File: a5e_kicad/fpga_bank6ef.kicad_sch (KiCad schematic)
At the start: 1 part, among them U7 A5EB013B-B23B

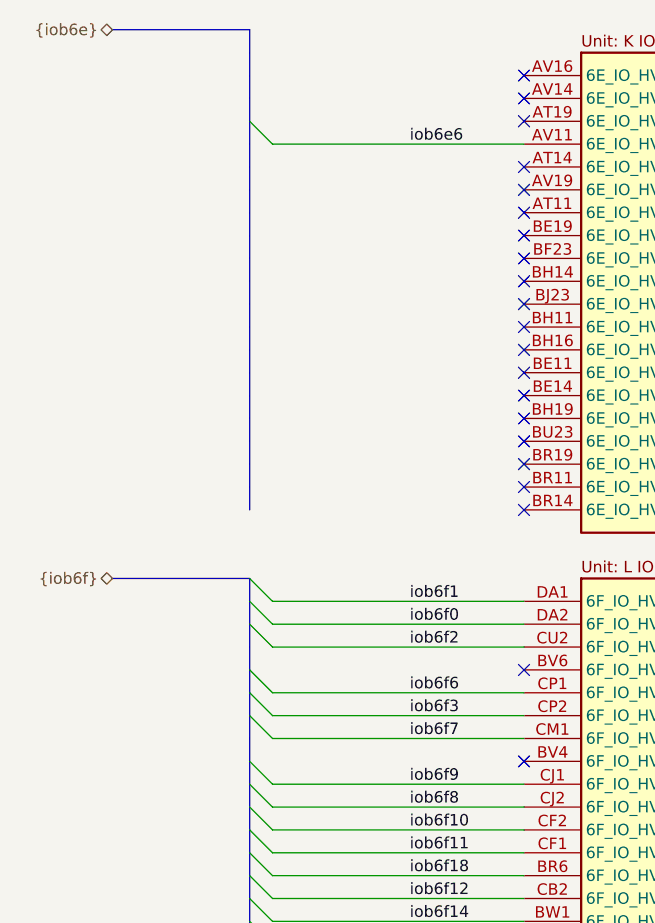
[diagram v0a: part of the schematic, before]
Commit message: Ethernet PHY passives to 0201, R27/R28 to 0402, preliminary RGMII routing
- 31 PHY passives on the hps_ethernet sheet 0402 -> 0201 (C24 22u stays
  0402): 100n C190183, 1u C272877, 27p C85899, 10k C473048,
  330R C516485, 4K7 C270346, 1K5 C270361, 2K49 C473476.
- Refclk bias R27/R28 0201 -> 0402 (C25120, 49.9R); R28 moved 0.1 mm
  to +x to clear the refclk_N meander.
- Preliminary RGMII routing: RX on F.Cu, TX on In2. Group spread
  TX 79 ps (TXD1 longest), RX 44 ps.
- Schematic sheets as saved by eeschema.
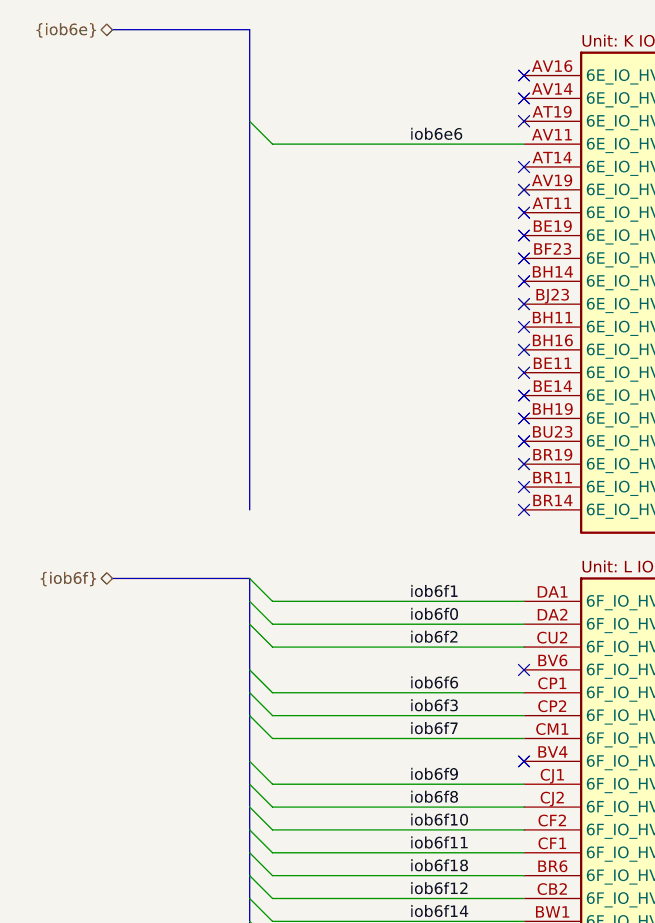
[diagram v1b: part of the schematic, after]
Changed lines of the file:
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@@
 	)
 	(no_connect
+		(at 96.52 66.04)
+	)
+	(no_connect
+		(at 96.52 58.42)
+	)
+	(no_connect
+		(at 96.52 60.96)
+	)
+	(no_connect
+		(at 96.52 50.8)
+	)
+	(no_connect
+		(at 96.52 45.72)
+	)
+	(no_connect
+		(at 96.52 55.88)
+	)
+	(no_connect
+		(at 96.52 71.12)
+	)
+	(no_connect
 		(at 96.52 129.54)
 	)
+	(no_connect
+		(at 96.52 93.98)
+	)
+	(no_connect
+		(at 96.52 48.26)
+	)
+	(no_connect
+		(at 96.52 73.66)
+	)
+	(no_connect
+		(at 96.52 30.48)
+	)
+	(no_connect
+		(at 96.52 38.1)
+	)
+	(no_connect
+		(at 96.52 40.64)
+	)
+	(no_connect
+		(at 96.52 53.34)
+	)
+	(no_connect
+		(at 96.52 104.14)
+	)
+	(no_connect
+		(at 96.52 68.58)
+	)
+	(no_connect
+		(at 96.52 33.02)
+	)
+	(no_connect
+		(at 96.52 27.94)
+	)
+	(no_connect
+		(at 96.52 43.18)
+	)
+	(no_connect
+		(at 96.52 63.5)
+	)
+	(no_connect
+		(at 96.52 76.2)
+	)
 	(bus_entry
 		(at 66.04 99.06)
@@
 	(bus
 		(pts
-			(xy 66.04 53.34) (xy 66.04 55.88)
-		)
-		(stroke
-			(width 0)
-			(type default)
-		)
-	)
-	(bus
-		(pts
 			(xy 66.04 132.08) (xy 66.04 137.16)
 		)
@@
 	(bus
 		(pts
-			(xy 66.04 66.04) (xy 66.04 68.58)
-		)
-		(stroke
-			(width 0)
-			(type default)
-		)
-	)
-	(bus
-		(pts
-			(xy 66.04 101.6) (xy 66.04 104.14)
+			(xy 66.04 99.06) (xy 66.04 104.14)
 		)
 		(stroke
@@
 		)
 	)
-	(bus
-		(pts
-			(xy 66.04 50.8) (xy 66.04 53.34)
-		)
-		(stroke
-			(width 0)
-			(type default)
-		)
-	)
-	(bus
-		(pts
-			(xy 66.04 45.72) (xy 66.04 48.26)
-		)
-		(stroke
-			(width 0)
-			(type default)
-		)
-	)
-	(bus
-		(pts
-			(xy 66.04 58.42) (xy 66.04 60.96)
-		)
-		(stroke
-			(width 0)
-			(type default)
-		)
-	)
 	(wire
 		(pts
@@
 		)
 	)
-	(bus
-		(pts
-			(xy 66.04 60.96) (xy 66.04 63.5)
-		)
-		(stroke
-			(width 0)
-			(type default)
-		)
-	)
 	(wire
 		(pts
@@
 		)
 	)
-	(bus
-		(pts
-			(xy 66.04 48.26) (xy 66.04 50.8)
-		)
-		(stroke
-			(width 0)
-			(type default)
-		)
-	)
 	(wire
 		(pts
@@
 		)
 	)
-	(bus
-		(pts
-			(xy 66.04 88.9) (xy 66.04 91.44)
-		)
-		(stroke
-			(width 0)
-			(type default)
-		)
-	)
-	(bus
-		(pts
-			(xy 66.04 22.86) (xy 66.04 25.4)
-		)
-		(stroke
-			(width 0)
-			(type default)
-		)
-	)
 	(wire
 		(pts
@@
 	(bus
 		(pts
-			(xy 66.04 30.48) (xy 66.04 33.02)
-		)
-		(stroke
-			(width 0)
-			(type default)
-		)
-	)
-	(bus
-		(pts
 			(xy 66.04 104.14) (xy 66.04 106.68)
 		)
@@
 	(bus
 		(pts
-			(xy 66.04 91.44) (xy 66.04 93.98)
-		)
-		(stroke
-			(width 0)
-			(type default)
-		)
-	)
-	(bus
-		(pts
-			(xy 66.04 43.18) (xy 66.04 45.72)
+			(xy 66.04 88.9) (xy 66.04 93.98)
 		)
 		(stroke
@@
 	(bus
 		(pts
-			(xy 66.04 73.66) (xy 66.04 76.2)
-		)
-		(stroke
-			(width 0)
-			(type default)
-		)
-	)
-	(bus
-		(pts
 			(xy 66.04 129.54) (xy 66.04 132.08)
 		)
@@
 	(bus
 		(pts
-			(xy 66.04 27.94) (xy 66.04 30.48)
-		)
-		(stroke
-			(width 0)
-			(type default)
-		)
-	)
-	(bus
-		(pts
 			(xy 66.04 86.36) (xy 66.04 88.9)
 		)
@@
 		)
 	)
-	(bus
-		(pts
-			(xy 66.04 55.88) (xy 66.04 58.42)
-		)
-		(stroke
-			(width 0)
-			(type default)
-		)
-	)
 	(wire
 		(pts
@@
 		)
 	)
-	(bus
-		(pts
-			(xy 66.04 68.58) (xy 66.04 71.12)
-		)
-		(stroke
-			(width 0)
-			(type default)
-		)
-	)
 	(wire
 		(pts
@@
 		)
 	)
-	(bus
-		(pts
-			(xy 66.04 63.5) (xy 66.04 66.04)
-		)
-		(stroke
-			(width 0)
-			(type default)
-		)
-	)
 	(wire
 		(pts
@@
 	(bus
 		(pts
-			(xy 66.04 38.1) (xy 66.04 40.64)
-		)
-		(stroke
-			(width 0)
-			(type default)
-		)
-	)
-	(bus
-		(pts
 			(xy 66.04 93.98) (xy 66.04 96.52)
 		)
@@
 	(bus
 		(pts
-			(xy 66.04 35.56) (xy 66.04 38.1)
-		)
-		(stroke
-			(width 0)
-			(type default)
-		)
-	)
-	(bus
-		(pts
 			(xy 66.04 119.38) (xy 66.04 121.92)
 		)
@@
 	(bus
 		(pts
-			(xy 66.04 99.06) (xy 66.04 101.6)
-		)
-		(stroke
-			(width 0)
-			(type default)
-		)
-	)
-	(bus
-		(pts
-			(xy 66.04 71.12) (xy 66.04 73.66)
-		)
-		(stroke
-			(width 0)
-			(type default)
-		)
-	)
-	(bus
-		(pts
-			(xy 66.04 25.4) (xy 66.04 27.94)
+			(xy 66.04 22.86) (xy 66.04 33.02)
 		)
 		(stroke
@@
 	(bus
 		(pts
-			(xy 66.04 40.64) (xy 66.04 43.18)
-		)
-		(stroke
-			(width 0)
-			(type default)
-		)
-	)
-	(bus
-		(pts
-			(xy 66.04 33.02) (xy 66.04 35.56)
+			(xy 66.04 33.02) (xy 66.04 76.2)
 		)
 		(stroke
@@
 		)
 	)
-	(no_connect
-		(at 96.52 104.14)
-	)
-	(no_connect
-		(at 96.52 66.04)
-	)
-	(no_connect
-		(at 96.52 38.1)
-	)
-	(no_connect
-		(at 96.52 43.18)
-	)
-	(no_connect
-		(at 96.52 93.98)
-	)
-	(no_connect
-		(at 96.52 55.88)
-	)
-	(no_connect
-		(at 96.52 33.02)
-	)
-	(no_connect
-		(at 96.52 40.64)
-	)
-	(no_connect
-		(at 96.52 27.94)
-	)
-	(no_connect
-		(at 96.52 76.2)
-	)
-	(no_connect
-		(at 96.52 53.34)
-	)
-	(no_connect
-		(at 96.52 50.8)
-	)
-	(no_connect
-		(at 96.52 45.72)
-	)
-	(no_connect
-		(at 96.52 63.5)
-	)
-	(no_connect
-		(at 96.52 48.26)
-	)
-	(no_connect
-		(at 96.52 73.66)
-	)
-	(no_connect
-		(at 96.52 30.48)
-	)
-	(no_connect
-		(at 96.52 58.42)
-	)
-	(no_connect
-		(at 96.52 71.12)
-	)
-	(no_connect
-		(at 96.52 68.58)
-	)
-	(no_connect
-		(at 96.52 60.96)
-	)
 )
